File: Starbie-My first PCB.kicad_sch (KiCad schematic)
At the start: 12 parts, among them J1 Conn_01x04_Pin, J2 Conn_01x02_Pin, J3 Conn_01x08_Pin, Q1 Q_NPN_CBE, SW1 SW_Push, SW2 SW_Push, U1 XIAO-ESP32-C3-SMD, U2 DHT11

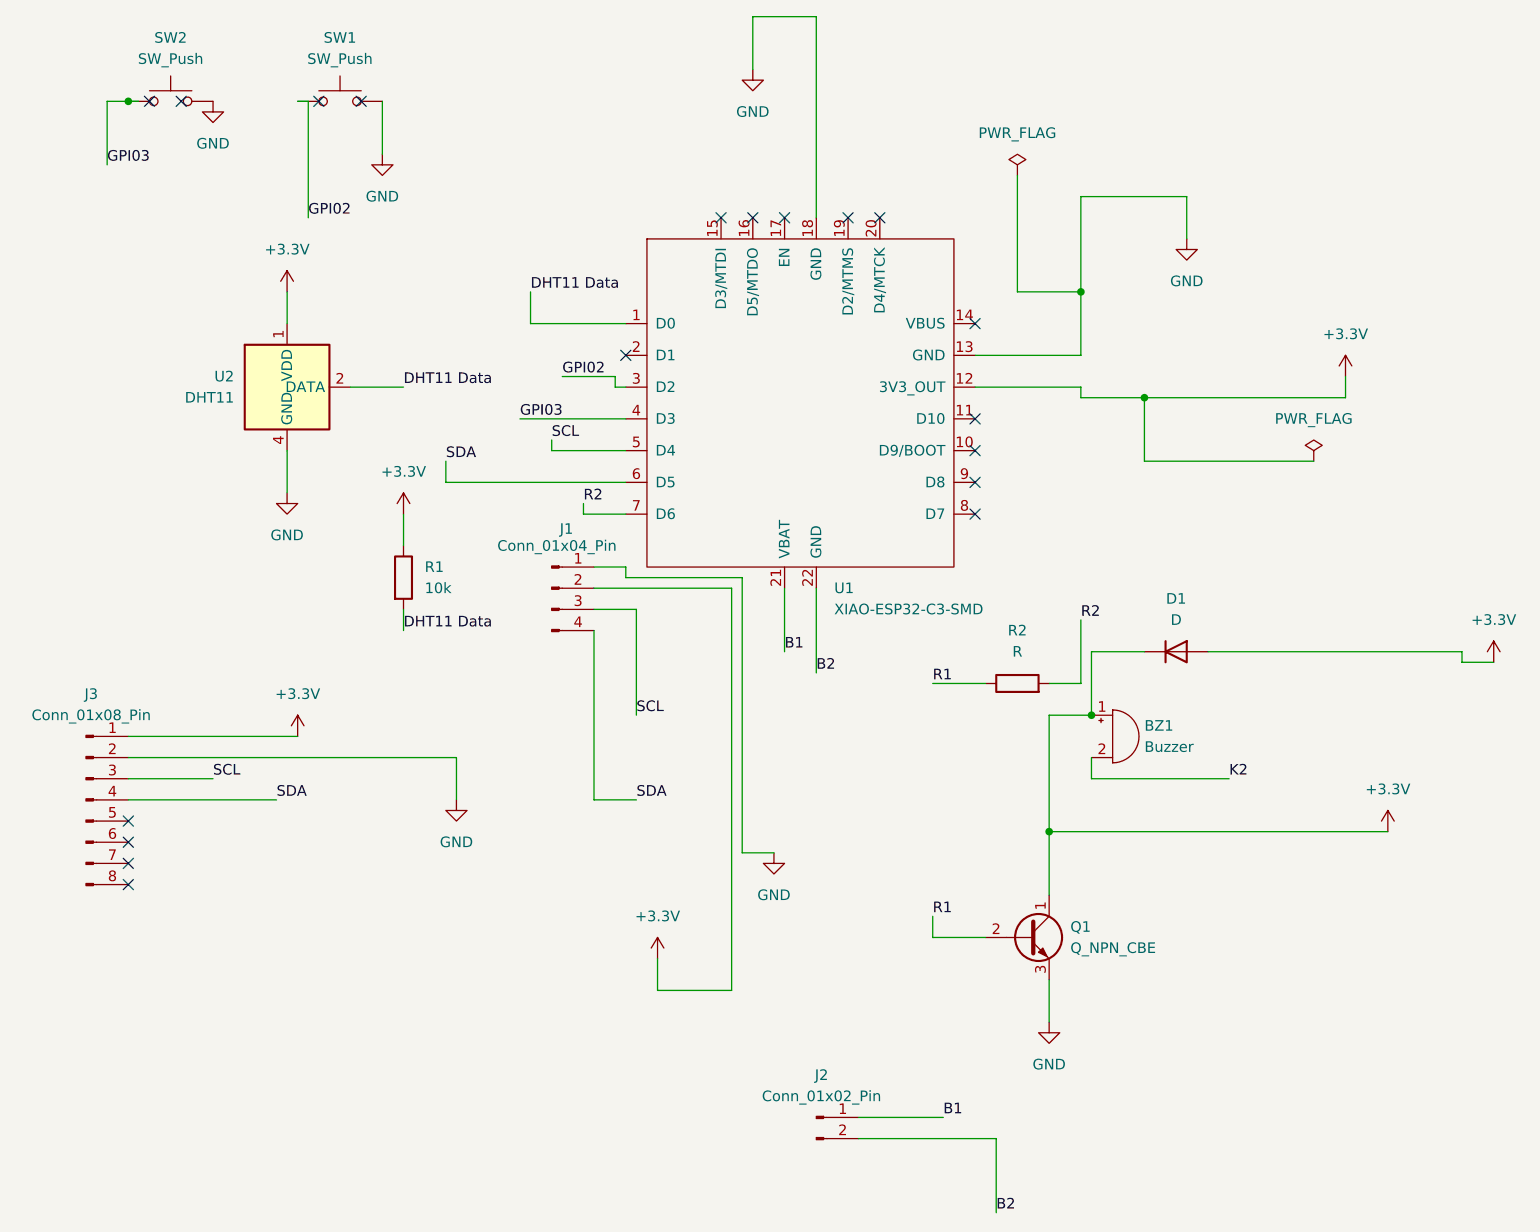
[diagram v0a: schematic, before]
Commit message: fix buzzer circuit and schematic erc warnings
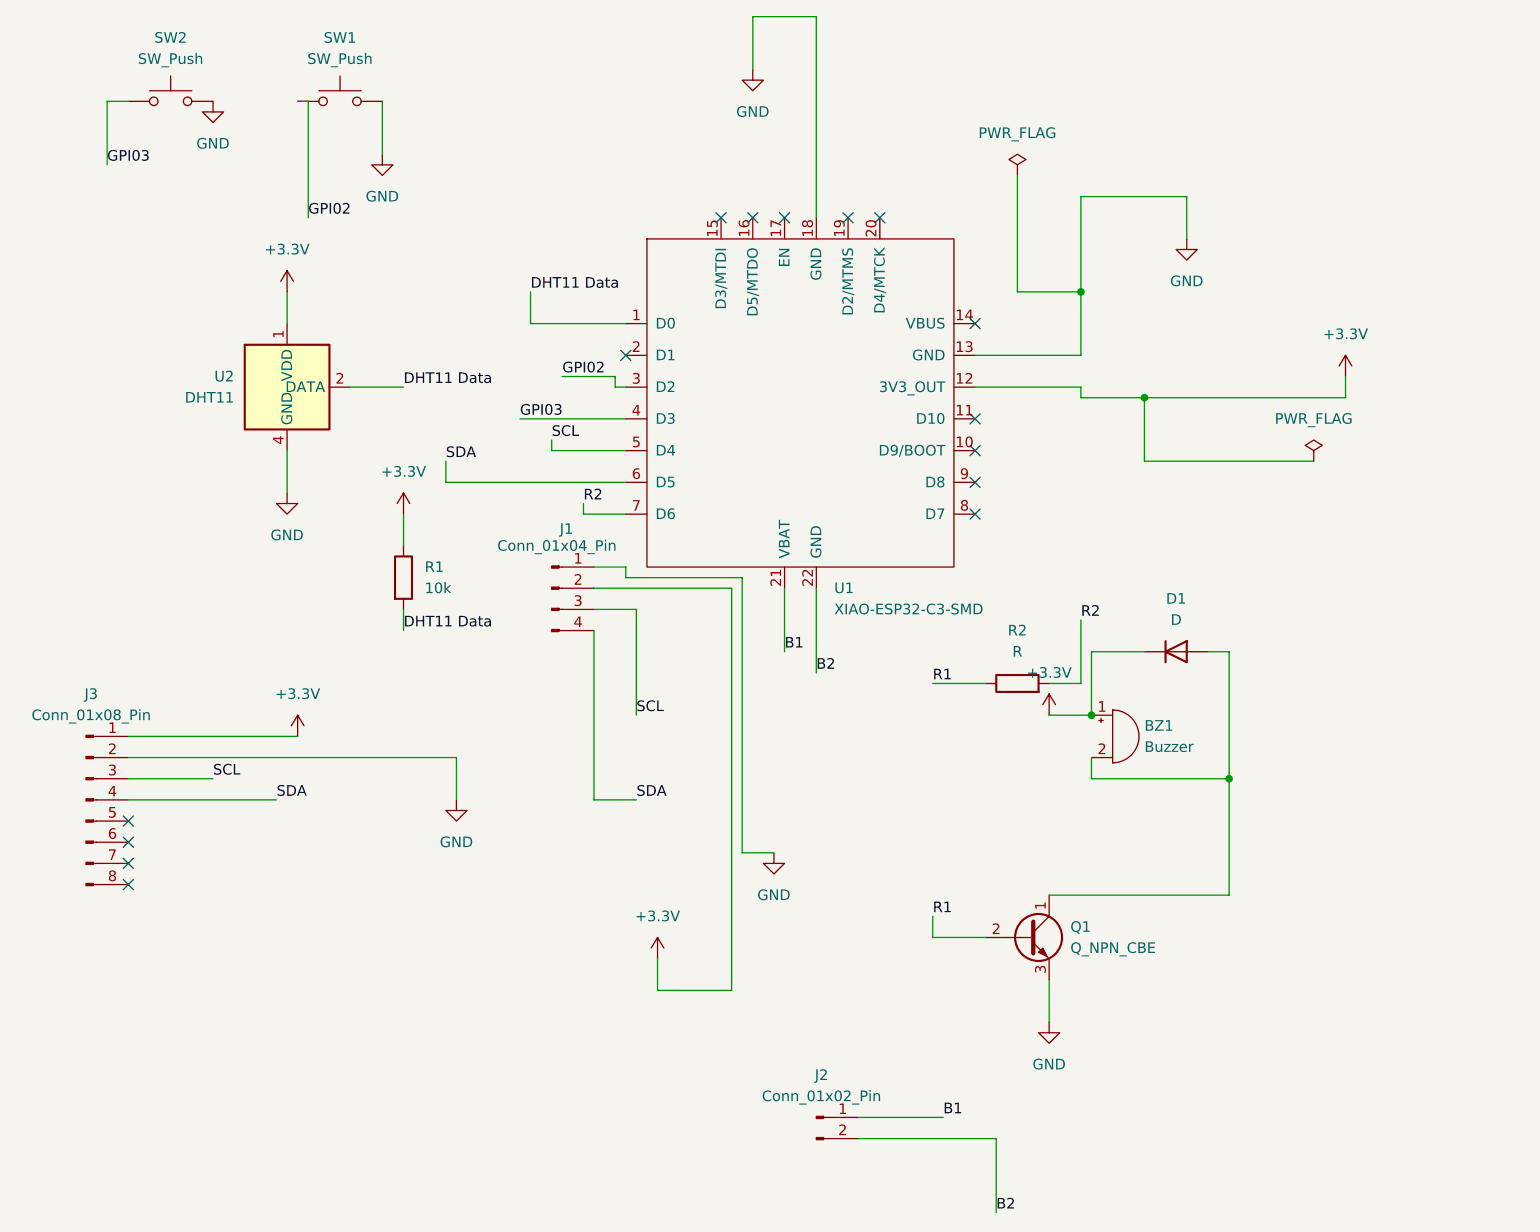
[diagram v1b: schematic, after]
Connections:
- net +3.3V: no longer D1.2 (A), Q1.1 (C)
- net K2: no longer names the net of BZ1.2 (-)
- net K2: now also D1.2 (A), Q1.1 (C)
- no-connect marks 19 -> 15
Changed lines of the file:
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@@
 	)
 	(junction
-		(at 146.05 124.46)
-		(diameter 0)
-		(color 0 0 0 0)
-	)
-	(junction
 		(at 151.13 110.49)
 		(diameter 0)
@@
 	)
 	(junction
-		(at 35.56 36.83)
+		(at 157.48 72.39)
 		(diameter 0)
 		(color 0 0 0 0)
 	)
 	(junction
-		(at 157.48 72.39)
+		(at 167.64 118.11)
 		(diameter 0)
 		(color 0 0 0 0)
@@
 	)
 	(no_connect
-		(at 38.1 36.83)
-	)
-	(no_connect
 		(at 35.56 123.19)
 	)
 	(no_connect
-		(at 41.91 36.83)
-	)
-	(no_connect
-		(at 58.42 36.83)
-	)
-	(no_connect
-		(at 63.5 36.83)
-	)
-	(no_connect
 		(at 137.16 74.93)
 	)
 	(wire
 		(pts
-			(xy 146.05 124.46) (xy 186.69 124.46)
-		)
-		(stroke
-			(width 0)
-			(type default)
-		)
-	)
-	(wire
-		(pts
 			(xy 146.05 106.68) (xy 149.86 106.68)
 		)
@@
 	(wire
 		(pts
-			(xy 195.58 104.14) (xy 199.39 104.14)
-		)
-		(stroke
-			(width 0)
-			(type default)
-		)
-	)
-	(wire
-		(pts
 			(xy 54.61 78.74) (xy 54.61 83.82)
 		)
@@
 	(wire
 		(pts
-			(xy 165.1 102.87) (xy 195.58 102.87)
-		)
-		(stroke
-			(width 0)
-			(type default)
-		)
-	)
-	(wire
-		(pts
 			(xy 57.15 36.83) (xy 57.15 50.8)
 		)
@@
 	(wire
 		(pts
-			(xy 146.05 110.49) (xy 146.05 124.46)
-		)
-		(stroke
-			(width 0)
-			(type default)
-		)
-	)
-	(wire
-		(pts
 			(xy 91.44 95.25) (xy 107.95 95.25)
 		)
@@
 	(wire
 		(pts
-			(xy 146.05 124.46) (xy 146.05 132.08)
-		)
-		(stroke
-			(width 0)
-			(type default)
-		)
-	)
-	(wire
-		(pts
 			(xy 110.49 26.67) (xy 118.11 26.67)
 		)
@@
 	(wire
 		(pts
-			(xy 36.83 36.83) (xy 35.56 36.83)
-		)
-		(stroke
-			(width 0)
-			(type default)
-		)
-	)
-	(wire
-		(pts
 			(xy 123.19 158.75) (xy 133.35 158.75)
 		)
@@
 	(wire
 		(pts
-			(xy 195.58 102.87) (xy 195.58 104.14)
-		)
-		(stroke
-			(width 0)
-			(type default)
-		)
-	)
-	(wire
-		(pts
 			(xy 73.66 82.55) (xy 73.66 80.01)
 		)
@@
 		)
 	)
-	(label "B1"
-		(at 114.3 102.87 0)
-		(effects
-			(font
-				(size 1.27 1.27)
-			)
-			(justify left bottom)
+	(wire
+		(pts
+			(xy 165.1 102.87) (xy 167.64 102.87)
+		)
+		(stroke
+			(width 0)
+			(type default)
 		)
 	)
-	(label "K2"
-		(at 167.64 118.11 0)
+	(wire
+		(pts
+			(xy 167.64 102.87) (xy 167.64 118.11)
+		)
+		(stroke
+			(width 0)
+			(type default)
+		)
+	)
+	(wire
+		(pts
+			(xy 167.64 118.11) (xy 167.64 132.08)
+		)
+		(stroke
+			(width 0)
+			(type default)
+		)
+	)
+	(wire
+		(pts
+			(xy 167.64 132.08) (xy 146.05 132.08)
+		)
+		(stroke
+			(width 0)
+			(type default)
+		)
+	)
+	(label "B1"
+		(at 114.3 102.87 0)
 		(effects
 			(font
@@
 	(symbol
 		(lib_id "power:+3.3V")
-		(at 199.39 104.14 0)
-		(unit 1)
-		(body_style 1)
-		(exclude_from_sim no)
-		(in_bom yes)
-		(on_board yes)
-		(in_pos_files yes)
-		(dnp no)
-		(fields_autoplaced yes)
-		(property "Reference" "#PWR012"
-			(at 199.39 107.95 0)
-			(hide yes)
-			(show_name no)
-			(do_not_autoplace no)
-			(effects
-				(font
-					(size 1.27 1.27)
-				)
-			)
-		)
-		(property "Value" "+3.3V"
-			(at 199.39 99.06 0)
-			(show_name no)
-			(do_not_autoplace no)
-			(effects
-				(font
-					(size 1.27 1.27)
-				)
-			)
-		)
-		(property "Footprint" ""
-			(at 199.39 104.14 0)
-			(hide yes)
-			(show_name no)
-			(do_not_autoplace no)
-			(effects
-				(font
-					(size 1.27 1.27)
-				)
-			)
-		)
-		(property "Datasheet" ""
-			(at 199.39 104.14 0)
-			(hide yes)
-			(show_name no)
-			(do_not_autoplace no)
-			(effects
-				(font
-					(size 1.27 1.27)
-				)
-			)
-		)
-		(property "Description" "Power symbol creates a global label with name \"+3.3V\""
-			(at 199.39 104.14 0)
-			(hide yes)
-			(show_name no)
-			(do_not_autoplace no)
-			(effects
-				(font
-					(size 1.27 1.27)
-				)
-			)
-		)
-		(pin "1"
-		)
-		(instances
-			(project "Starbie-My first PCB"
-				(path "/462a7c6b-186c-4359-85c7-38a8bde0fd0c"
-					(reference "#PWR012")
-					(unit 1)
-				)
-			)
-		)
-	)
-	(symbol
-		(lib_id "power:+3.3V")
-		(at 186.69 124.46 0)
+		(at 146.05 110.49 0)
 		(unit 1)
 		(body_style 1)
@@
 		(fields_autoplaced yes)
 		(property "Reference" "#PWR015"
-			(at 186.69 128.27 0)
+			(at 146.05 114.30 0)
 			(hide yes)
 			(show_name no)
@@
 		)
 		(property "Value" "+3.3V"
-			(at 186.69 119.38 0)
+			(at 146.05 105.41 0)
 			(show_name no)
 			(do_not_autoplace no)
@@
 		)
 		(property "Footprint" ""
-			(at 186.69 124.46 0)
+			(at 146.05 110.49 0)
 			(hide yes)
 			(show_name no)
@@
 		)
 		(property "Datasheet" ""
-			(at 186.69 124.46 0)
+			(at 146.05 110.49 0)
 			(hide yes)
 			(show_name no)
@@
 		)
 		(property "Description" "Power symbol creates a global label with name \"+3.3V\""
-			(at 186.69 124.46 0)
+			(at 146.05 110.49 0)
 			(hide yes)
 			(show_name no)
